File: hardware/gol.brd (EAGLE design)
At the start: 67.3 x 67.3 mm, 70 parts, among them J1 TC2050-IDC, J2 2057-MCR-B-S-RA-TSMT-NP-CS4-T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, U1 STM32F072CBT, U2 AP2111H-3.3TRG1SOT-223_DIO-M

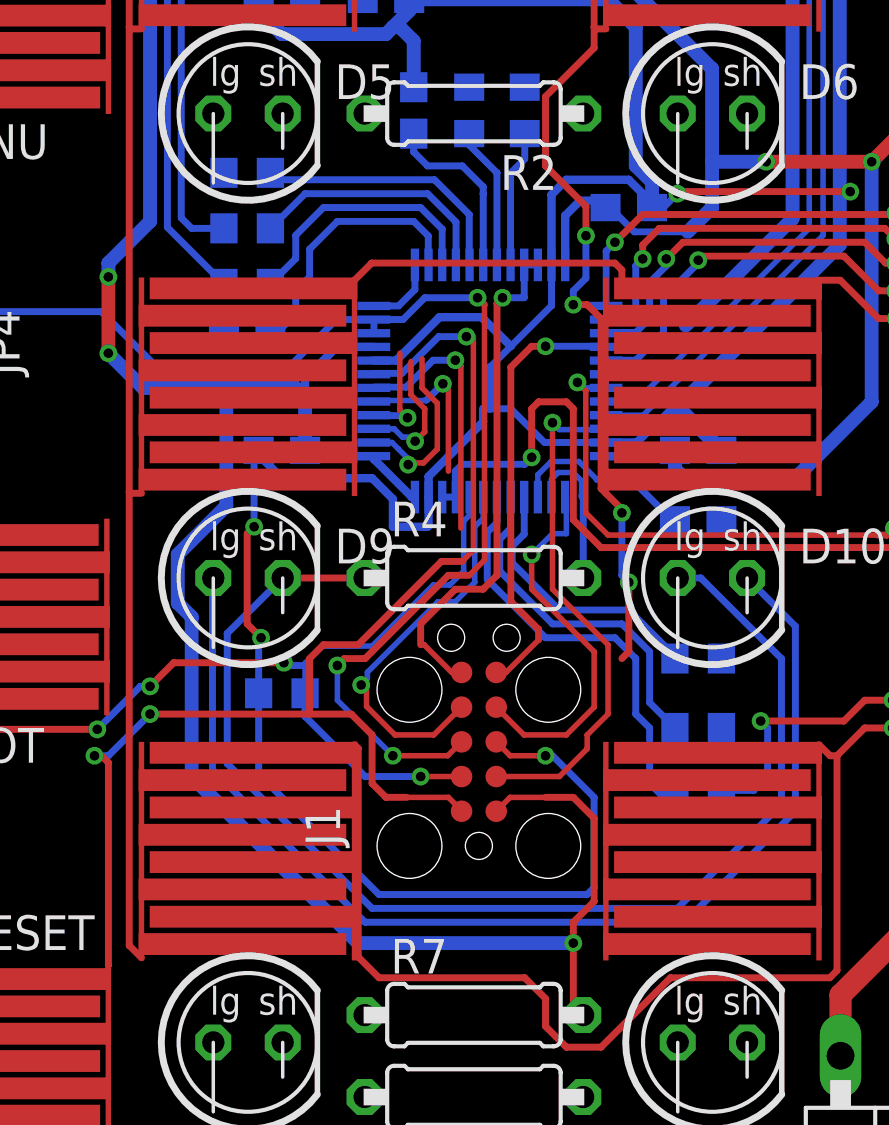
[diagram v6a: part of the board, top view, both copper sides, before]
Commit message: Prep for rearranging the capacitive inputs.
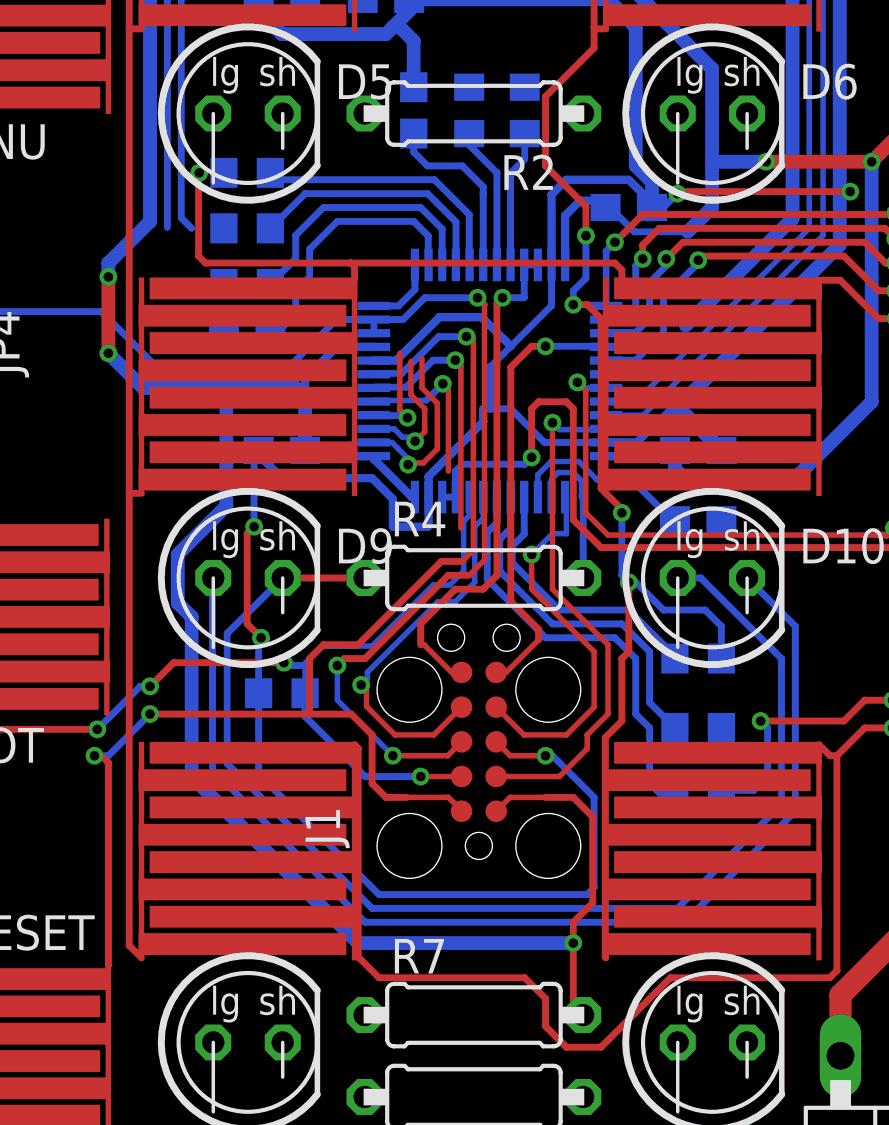
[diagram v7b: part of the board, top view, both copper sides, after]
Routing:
- net IN_COL1: track 49.9 -> 66.3 mm
- net IN_ROW2: track 49.4 -> 58.7 mm, vias 2 -> 3
- net IN_ROW0: track 111.4 -> 108.4 mm
- net IN_ROW1: track 81.5 -> 80.3 mm
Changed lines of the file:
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@@
 <wire x1="34.0868" y1="52.0192" x2="18.9992" y2="52.0192" width="0.508" layer="1"/>
 <wire x1="23.622" y1="13.97" x2="24.638" y2="13.97" width="0.254" layer="1"/>
-<wire x1="24.638" y1="13.97" x2="25.4" y2="13.208" width="0.254" layer="1"/>
-<wire x1="25.4" y1="10.16" x2="24.638" y2="9.398" width="0.254" layer="1"/>
+<wire x1="24.638" y1="13.97" x2="25.3492" y2="13.2588" width="0.254" layer="1"/>
+<wire x1="25.3492" y1="10.1092" x2="24.638" y2="9.398" width="0.254" layer="1"/>
 <wire x1="24.638" y1="6.362" x2="24.638" y2="8.636" width="0.254" layer="1"/>
 <wire x1="24.638" y1="6.362" x2="25" y2="6" width="0.254" layer="1"/>
-<wire x1="25.4" y1="13.208" x2="25.4" y2="10.16" width="0.254" layer="1"/>
+<wire x1="25.3492" y1="13.2588" x2="25.3492" y2="10.1092" width="0.254" layer="1"/>
 <wire x1="24.638" y1="9.398" x2="24.638" y2="8.636" width="0.254" layer="1"/>
 <via x="24.638" y="8.636" extent="1-16" drill="0.35"/>
@@
 <contactref element="BTN4" pad="P$2"/>
 <contactref element="R11" pad="2"/>
-<wire x1="11.85" y1="32.766" x2="9.779" y2="34.837" width="0.254" layer="16"/>
 <wire x1="9.779" y1="50.9778" x2="9.9314" y2="51.1302" width="0.254" layer="16"/>
 <wire x1="9.9314" y1="51.1302" x2="9.9314" y2="51.4759875" width="0.254" layer="16"/>
@@
 <wire x1="58.83" y1="66.392" x2="58.293" y2="66.929" width="0.254" layer="1"/>
 <wire x1="58.293" y1="66.929" x2="53.467" y2="66.929" width="0.254" layer="1"/>
+<wire x1="9.779" y1="34.837" x2="11.85" y2="32.766" width="0" layer="19" extent="16-16"/>
 </signal>
 <signal name="IN_ROW1">
@@
 <wire x1="35.433" y1="47.625" x2="35.7632" y2="47.2948" width="0.254" layer="1"/>
 <wire x1="41.91" y1="50.546" x2="50.546" y2="50.546" width="0.254" layer="1"/>
-<wire x1="10.668" y1="34.798" x2="11.85" y2="34.798" width="0.254" layer="16"/>
+<wire x1="10.668" y1="34.798" x2="11.85" y2="34.798" width="0" layer="19" extent="16-16"/>
 </signal>
 <signal name="IN_ROW2">
@@
 <wire x1="41.656" y1="31.496" x2="42.164" y2="32.004" width="0.254" layer="16"/>
 <wire x1="42.164" y1="33.528" x2="50.546" y2="33.528" width="0.254" layer="1"/>
-<wire x1="16.63" y1="32.9" x2="17.258" y2="33.528" width="0.254" layer="1"/>
-<wire x1="26.162" y1="33.528" x2="17.258" y2="33.528" width="0.254" layer="1"/>
+<wire x1="16.63" y1="32.9" x2="16.63" y2="33.394" width="0.254" layer="1"/>
+<wire x1="16.63" y1="33.394" x2="16.496" y2="33.528" width="0.254" layer="1"/>
+<wire x1="26.162" y1="33.528" x2="16.496" y2="33.528" width="0.254" layer="1"/>
 <wire x1="33.63" y1="32.9" x2="33.496" y2="32.766" width="0.254" layer="1"/>
 <wire x1="26.416" y1="33.274" x2="26.162" y2="33.528" width="0.254" layer="1"/>
 <wire x1="33.496" y1="32.766" x2="26.416" y2="32.766" width="0.254" layer="1"/>
 <wire x1="26.416" y1="32.766" x2="26.416" y2="33.274" width="0.254" layer="1"/>
-<wire x1="16.63" y1="32.9" x2="11.85" y2="36.83" width="0" layer="19" extent="1-16"/>
+<via x="10.9446" y="36.83" extent="1-16" drill="0.35"/>
+<wire x1="10.9446" y1="36.83" x2="10.922" y2="36.8074" width="0.254" layer="1"/>
+<wire x1="10.922" y1="36.8074" x2="10.922" y2="33.782" width="0.254" layer="1"/>
+<wire x1="10.922" y1="33.782" x2="11.176" y2="33.528" width="0.254" layer="1"/>
+<wire x1="11.176" y1="33.528" x2="16.496" y2="33.528" width="0.254" layer="1"/>
+<wire x1="10.9446" y1="36.83" x2="11.85" y2="36.83" width="0" layer="19" extent="16-16"/>
 </signal>
 <signal name="IN_ROW3">
@@
 <wire x1="26.67" y1="21.844" x2="26.67" y2="19.304" width="0.254" layer="1"/>
 <wire x1="26.67" y1="19.304" x2="26.416" y2="19.05" width="0.254" layer="1"/>
-<wire x1="26.416" y1="19.05" x2="30.06" y2="19.05" width="0" layer="19" extent="1-16"/>
-<wire x1="25.83" y1="8.1" x2="26.416" y2="19.05" width="0" layer="19" extent="1-1"/>
+<wire x1="30.06" y1="19.05" x2="30.06" y2="20.232" width="0.254" layer="16"/>
+<wire x1="26.924" y1="21.844" x2="26.67" y2="21.844" width="0.254" layer="16"/>
+<wire x1="30.06" y1="20.232" x2="29.464" y2="20.828" width="0.254" layer="16"/>
+<wire x1="29.464" y1="20.828" x2="27.94" y2="20.828" width="0.254" layer="16"/>
+<wire x1="27.94" y1="20.828" x2="26.924" y2="21.844" width="0.254" layer="16"/>
+<wire x1="26.416" y1="16.764" x2="26.416" y2="19.05" width="0.254" layer="1"/>
+<wire x1="25.83" y1="8.1" x2="25.8064" y2="8.1236" width="0.254" layer="1"/>
+<wire x1="25.8064" y1="8.1236" x2="25.8064" y2="16.1544" width="0.254" layer="1"/>
+<wire x1="25.8064" y1="16.1544" x2="26.416" y2="16.764" width="0.254" layer="1"/>
 </signal>
 <signal name="IN_COL2">

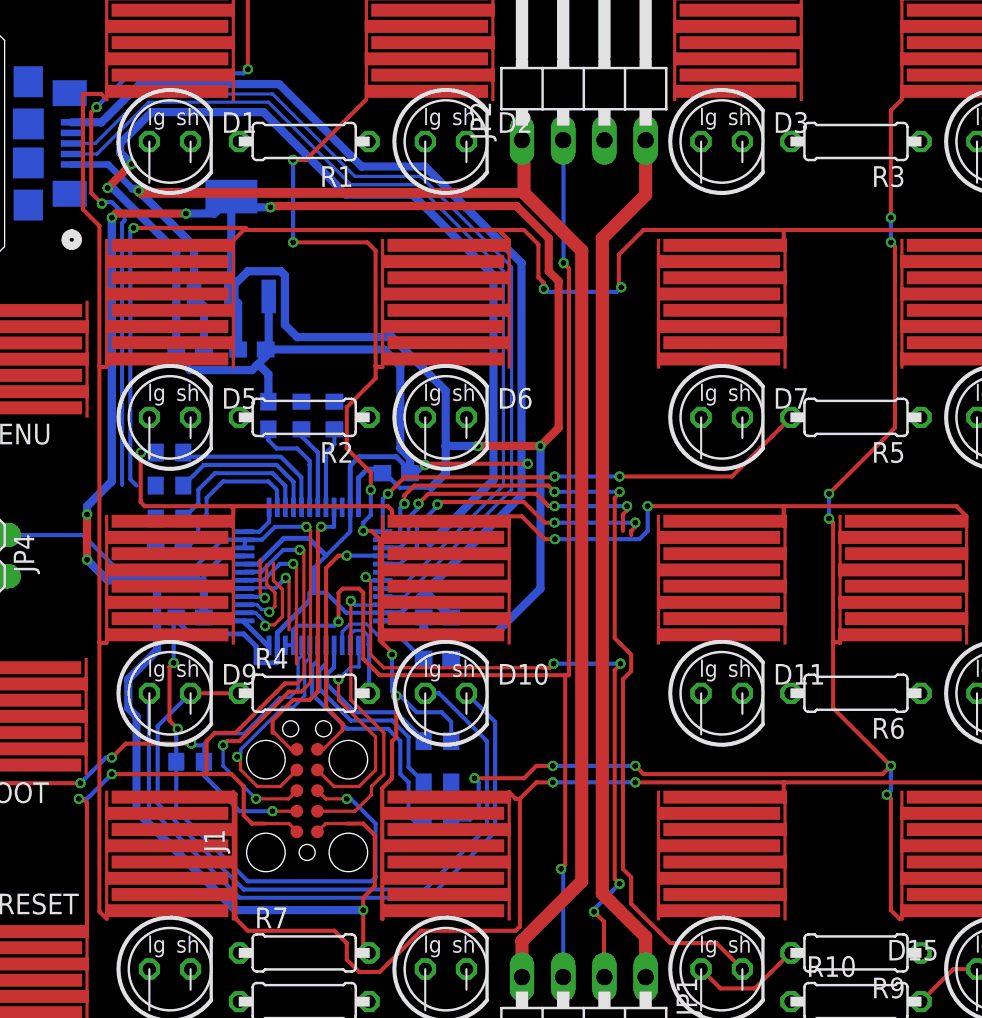
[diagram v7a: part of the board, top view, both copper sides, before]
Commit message: Finishes rerouting the row/col ports
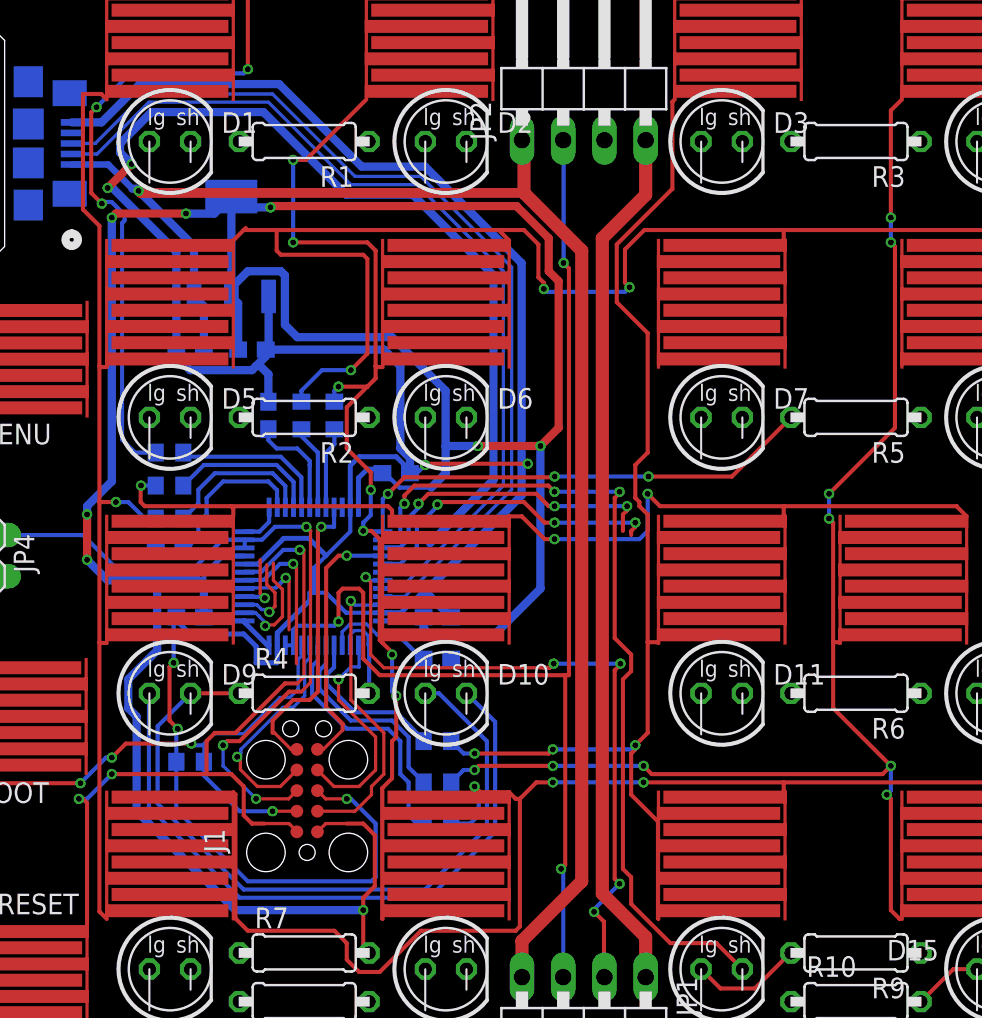
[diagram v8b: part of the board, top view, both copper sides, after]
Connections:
- net COL0: now also R11.1, U1.15; no longer R16.2, U1.20
- net COL1: now also R16.2, U1.20; no longer R17.2, U1.40
- net COL2: now also R17.2, U1.40; no longer R18.2, U1.41
- net COL3: now also R18.2, U1.41; no longer R19.2, U1.42
- net IN_COL0: now also R11.2; no longer R16.1
- net IN_COL1: now also R16.1; no longer R17.1
- net IN_COL2: now also R17.1; no longer R18.1
- net IN_COL3: now also R18.1; no longer R19.1
- net IN_ROW0: now also R14.2; no longer R11.2
- net IN_ROW1: now also R15.2; no longer R13.2
- net IN_ROW2: now also R13.2; no longer R14.2
- net IN_ROW3: now also R19.1; no longer R15.2
- net ROW0: now also R14.1, U1.17; no longer R11.1, U1.15
- net ROW1: now also R15.1, U1.19; no longer R13.1, U1.16
- net ROW2: now also R13.1, U1.16; no longer R14.1, U1.17
- net ROW3: now also R19.2, U1.42; no longer R15.1, U1.19
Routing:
- net IN_COL2: track 0.00 -> 67.1 mm, vias 0 -> 3
- net ROW3: track 5.23 -> 15.7 mm
- net IN_ROW3: track 70.1 -> 76.2 mm, vias 2 -> 3
- net COL1: track 10.0 -> 5.02 mm
- net COL0: track 5.02 -> 9.58 mm
- net ROW1: track 9.32 -> 5.23 mm
- net IN_ROW1: track 80.3 -> 76.2 mm
- net IN_COL0: track 54.0 -> 57.9 mm, vias 0 -> 1
- net COL3: track 15.7 -> 12.8 mm
- net COL2: track 12.8 -> 10.0 mm
- net IN_COL3: track 85.7 -> 83.1 mm
- net IN_COL1: track 66.3 -> 63.9 mm, vias 6 -> 7
